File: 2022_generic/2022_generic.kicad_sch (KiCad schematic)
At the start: 15 parts, among them J1 Screw_Terminal_01x02, J2 Programming Connector, SW1 6mm tactile button, U1 PIC16LF15313

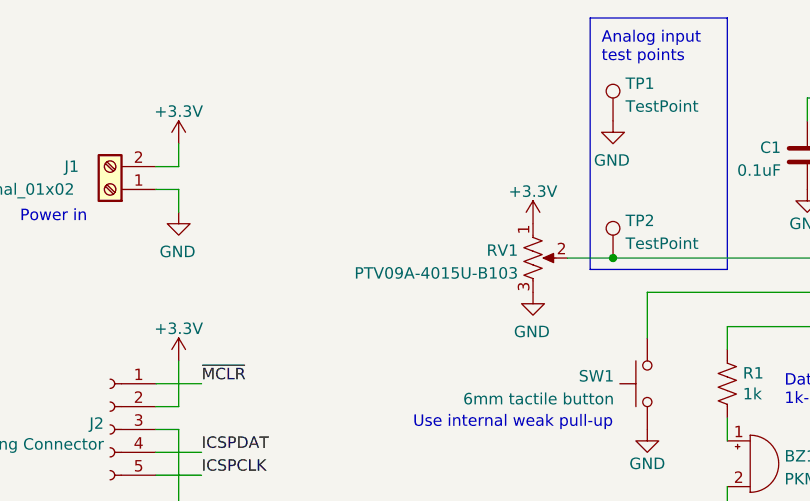
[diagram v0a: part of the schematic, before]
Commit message: Add pot explanation and test point numbers
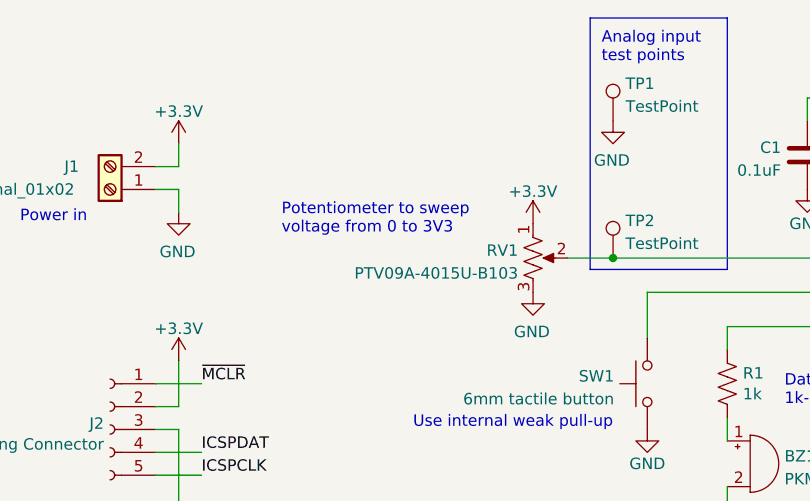
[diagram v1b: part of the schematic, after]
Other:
- note added: "Potentiometer to sweep voltage from 0 to 3V3"
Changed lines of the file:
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@@
+    (effects (font (size 1.27 1.27)) (justify left bottom))
+  )
+  (text "Potentiometer to sweep\nvoltage from 0 to 3V3" (at 101.6 90.17 0)
     (effects (font (size 1.27 1.27)) (justify left bottom))
   )

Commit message: Update PIC part number
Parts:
- U1: value PIC16LF15313 -> PIC12LF1501
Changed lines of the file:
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@@
     (in_bom yes) (on_board yes) (fields_autoplaced)
     (property "Reference" "U1" (id 0) (at 180.34 82.711 0))
-    (property "Value" "PIC16LF15313" (id 1) (at 180.34 85.2479 0))
+    (property "Value" "PIC12LF1501" (id 1) (at 180.34 85.2479 0))
     (property "Footprint" "Package_SO:SOIC-8_3.9x4.9mm_P1.27mm" (id 2) (at 177.165 95.885 0)
       (effects (font (size 1.27 1.27)) hide)
@@
     )
     (path "/a1b778f1-9434-43dc-b144-9735c1ab2243"
-      (reference "U1") (unit 1) (value "PIC16LF15313") (footprint "Package_SO:SOIC-8_3.9x4.9mm_P1.27mm")
-    )
-  )
+      (reference "U1") (unit 1) (value "PIC12LF1501") (footprint "Package_SO:SOIC-8_3.9x4.9mm_P1.27mm")
+    )
+  )
